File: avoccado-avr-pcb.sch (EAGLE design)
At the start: 32 parts, among them IC1 MCP1703CB, Q1 #MHz, Q2 MOSFET-NCHANNEL2N7002PW, U1 ATMEGA168#, U2 MCP73831, X1 Micro USB

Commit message: squeezed the headers together to make the PCB even thinner
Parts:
- removed C2: 0.1uF, SparkFun:CAP0402
- removed JP6, JP7: M12PTH, SparkFun:M12PTH
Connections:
- net A0: no longer JP6.8
- net A1: no longer JP6.7
- net A2: no longer JP6.6
- net A3: no longer JP6.5
- net D10: no longer JP6.12
- net D2: no longer JP7.8
- net D3: no longer JP7.7
- net D4: no longer JP7.6
- net D5-VIBR: no longer JP7.5
- net D6: no longer JP7.4
- net D7: no longer JP7.3
- net D8: no longer JP7.2
- net D9: no longer JP7.1
- net DTR: no longer C2.2
- net GND: no longer JP6.2, JP7.9
- net MISO: no longer JP6.10
- net MOSI: no longer JP6.11
- net RAW: no longer JP6.1
- net RESET: no longer C2.1, JP6.3, JP7.10
- net RXI: no longer JP7.11
- net SCK: no longer JP6.9
- net TXO: no longer JP7.12
- net VCC: no longer JP6.4
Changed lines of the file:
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@@
 <part name="U$2" library="SparkFun" deviceset="FIDUCIAL" device="1X2"/>
 <part name="U$4" library="SparkFun" deviceset="FIDUCIAL" device="1X2"/>
-<part name="JP6" library="SparkFun" deviceset="M12" device="PTH" value=""/>
-<part name="JP7" library="SparkFun" deviceset="M12" device="PTH" value=""/>
 <part name="Q1" library="SparkFun" deviceset="RESONATOR" device="SMD" value="#MHz"/>
 <part name="GND4" library="SparkFun" deviceset="GND" device=""/>
@@
 <part name="GND5" library="SparkFun" deviceset="GND" device=""/>
 <part name="JP1" library="SparkFun" deviceset="ARDUINO_SERIAL_PROGRAM" device="PTH" value="FTDI Basic"/>
-<part name="C2" library="SparkFun" deviceset="CAP" device="0402" value="0.1uF"/>
 <part name="Q2" library="SparkFun-DiscreteSemi" deviceset="MOSFET-NCHANNEL" device="2N7002PW"/>
 <part name="R1" library="SparkFun-Passives" deviceset="RESISTOR" device="0805-RES" value="1K"/>
@@
 <instance part="U$2" gate="G$1" x="236.22" y="25.4"/>
 <instance part="U$4" gate="G$1" x="241.3" y="25.4"/>
-<instance part="JP6" gate="G$1" x="134.62" y="58.42" rot="R180"/>
-<instance part="JP7" gate="G$1" x="48.26" y="60.96"/>
 <instance part="Q1" gate="G$1" x="165.1" y="127" smashed="yes" rot="MR90">
 <attribute name="NAME" x="162.306" y="123.444" size="1.778" layer="95" rot="MR180"/>
@@
 <instance part="GND5" gate="1" x="165.1" y="93.98"/>
 <instance part="JP1" gate="G$1" x="25.4" y="66.04"/>
-<instance part="C2" gate="G$1" x="132.08" y="154.94" smashed="yes" rot="R270">
-<attribute name="NAME" x="131.953" y="155.956" size="1.778" layer="95" rot="R90"/>
-<attribute name="VALUE" x="136.779" y="155.956" size="1.778" layer="96" rot="R90"/>
-</instance>
 <instance part="Q2" gate="G$1" x="48.26" y="104.14"/>
 <instance part="R1" gate="G$1" x="30.48" y="104.14"/>
@@
 <segment>
 <label x="78.74" y="66.04" size="1.778" layer="95"/>
-<pinref part="JP7" gate="G$1" pin="9"/>
 <wire x1="58.42" y1="66.04" x2="69.85" y2="66.04" width="0.1524" layer="91"/>
 <pinref part="JP11" gate="G$1" pin="1"/>
@@
 <segment>
 <label x="96.52" y="71.12" size="1.778" layer="95"/>
-<pinref part="JP6" gate="G$1" pin="2"/>
 <wire x1="124.46" y1="71.12" x2="110.49" y2="71.12" width="0.1524" layer="91"/>
 <pinref part="JP3" gate="G$1" pin="2"/>
@@
 <segment>
 <label x="78.74" y="68.58" size="1.778" layer="95"/>
-<pinref part="JP7" gate="G$1" pin="10"/>
 <wire x1="58.42" y1="68.58" x2="69.85" y2="68.58" width="0.1524" layer="91"/>
 <pinref part="JP11" gate="G$1" pin="2"/>
@@
 <segment>
 <label x="96.52" y="68.58" size="1.778" layer="95"/>
-<pinref part="JP6" gate="G$1" pin="3"/>
 <wire x1="124.46" y1="68.58" x2="110.49" y2="68.58" width="0.1524" layer="91"/>
 <pinref part="JP3" gate="G$1" pin="3"/>
@@
 <wire x1="167.64" y1="154.94" x2="142.24" y2="154.94" width="0.1524" layer="91"/>
 <wire x1="142.24" y1="157.48" x2="142.24" y2="154.94" width="0.1524" layer="91"/>
-<wire x1="142.24" y1="154.94" x2="137.16" y2="154.94" width="0.1524" layer="91"/>
-<junction x="142.24" y="154.94"/>
 <label x="152.4" y="154.94" size="1.778" layer="95"/>
 <pinref part="U1" gate="G$1" pin="PC6(/RESET)"/>
 <pinref part="R2" gate="G$1" pin="1"/>
-<pinref part="C2" gate="G$1" pin="1"/>
 </segment>
 </net>
@@
 <segment>
 <label x="96.52" y="53.34" size="1.778" layer="95"/>
-<pinref part="JP6" gate="G$1" pin="9"/>
 <wire x1="124.46" y1="53.34" x2="110.49" y2="53.34" width="0.1524" layer="91"/>
 <pinref part="JP8" gate="G$1" pin="1"/>
@@
 <segment>
 <label x="96.52" y="50.8" size="1.778" layer="95"/>
-<pinref part="JP6" gate="G$1" pin="10"/>
 <wire x1="124.46" y1="50.8" x2="110.49" y2="50.8" width="0.1524" layer="91"/>
 <pinref part="JP8" gate="G$1" pin="2"/>
@@
 <segment>
 <label x="96.52" y="48.26" size="1.778" layer="95"/>
-<pinref part="JP6" gate="G$1" pin="11"/>
 <wire x1="124.46" y1="48.26" x2="110.49" y2="48.26" width="0.1524" layer="91"/>
 <pinref part="JP8" gate="G$1" pin="3"/>
@@
 <segment>
 <label x="78.74" y="73.66" size="1.778" layer="95"/>
-<pinref part="JP7" gate="G$1" pin="12"/>
 <wire x1="58.42" y1="73.66" x2="69.85" y2="73.66" width="0.1524" layer="91"/>
 <pinref part="JP11" gate="G$1" pin="4"/>
@@
 <segment>
 <label x="96.52" y="66.04" size="1.778" layer="95"/>
-<pinref part="JP6" gate="G$1" pin="4"/>
 <wire x1="124.46" y1="66.04" x2="110.49" y2="66.04" width="0.1524" layer="91"/>
 <pinref part="JP3" gate="G$1" pin="4"/>
@@
 <segment>
 <label x="96.52" y="73.66" size="1.778" layer="95"/>
-<pinref part="JP6" gate="G$1" pin="1"/>
 <wire x1="124.46" y1="73.66" x2="110.49" y2="73.66" width="0.1524" layer="91"/>
 <pinref part="JP3" gate="G$1" pin="1"/>
@@
 <segment>
 <label x="78.74" y="45.72" size="1.778" layer="95"/>
-<pinref part="JP7" gate="G$1" pin="1"/>
 <wire x1="58.42" y1="45.72" x2="69.85" y2="45.72" width="0.1524" layer="91"/>
 <pinref part="JP9" gate="G$1" pin="1"/>
@@
 <segment>
 <label x="78.74" y="48.26" size="1.778" layer="95"/>
-<pinref part="JP7" gate="G$1" pin="2"/>
 <wire x1="83.82" y1="48.26" x2="69.85" y2="48.26" width="0.1524" layer="91"/>
 <pinref part="JP9" gate="G$1" pin="2"/>
@@
 <segment>
 <label x="96.52" y="63.5" size="1.778" layer="95"/>
-<pinref part="JP6" gate="G$1" pin="5"/>
 <wire x1="124.46" y1="63.5" x2="110.49" y2="63.5" width="0.1524" layer="91"/>
 <pinref part="JP5" gate="G$1" pin="1"/>
@@
 <segment>
 <label x="96.52" y="60.96" size="1.778" layer="95"/>
-<pinref part="JP6" gate="G$1" pin="6"/>
 <wire x1="124.46" y1="60.96" x2="110.49" y2="60.96" width="0.1524" layer="91"/>
 <pinref part="JP5" gate="G$1" pin="2"/>
@@
 <segment>
 <label x="96.52" y="58.42" size="1.778" layer="95"/>
-<pinref part="JP6" gate="G$1" pin="7"/>
 <wire x1="124.46" y1="58.42" x2="110.49" y2="58.42" width="0.1524" layer="91"/>
 <pinref part="JP5" gate="G$1" pin="3"/>
@@
 <segment>
 <label x="96.52" y="55.88" size="1.778" layer="95"/>
-<pinref part="JP6" gate="G$1" pin="8"/>
 <wire x1="124.46" y1="55.88" x2="110.49" y2="55.88" width="0.1524" layer="91"/>
 <pinref part="JP5" gate="G$1" pin="4"/>
@@
 <segment>
 <label x="78.74" y="63.5" size="1.778" layer="95"/>
-<pinref part="JP7" gate="G$1" pin="8"/>
 <wire x1="58.42" y1="63.5" x2="69.85" y2="63.5" width="0.1524" layer="91"/>
 <pinref part="JP10" gate="G$1" pin="4"/>
@@
 <segment>
 <label x="78.74" y="60.96" size="1.778" layer="95"/>
-<pinref part="JP7" gate="G$1" pin="7"/>
 <wire x1="83.82" y1="60.96" x2="69.85" y2="60.96" width="0.1524" layer="91"/>
 <pinref part="JP10" gate="G$1" pin="3"/>
@@
 <segment>
 <label x="78.74" y="58.42" size="1.778" layer="95"/>
-<pinref part="JP7" gate="G$1" pin="6"/>
 <wire x1="83.82" y1="58.42" x2="69.85" y2="58.42" width="0.1524" layer="91"/>
 <pinref part="JP10" gate="G$1" pin="2"/>
@@
 <segment>
 <label x="78.74" y="55.88" size="1.778" layer="95"/>
-<pinref part="JP7" gate="G$1" pin="5"/>
 <wire x1="58.42" y1="55.88" x2="69.85" y2="55.88" width="0.1524" layer="91"/>
 <pinref part="JP10" gate="G$1" pin="1"/>
@@
 <segment>
 <label x="78.74" y="53.34" size="1.778" layer="95"/>
-<pinref part="JP7" gate="G$1" pin="4"/>
 <wire x1="58.42" y1="53.34" x2="69.85" y2="53.34" width="0.1524" layer="91"/>
 <pinref part="JP9" gate="G$1" pin="4"/>
@@
 <segment>
 <label x="78.74" y="50.8" size="1.778" layer="95"/>
-<pinref part="JP7" gate="G$1" pin="3"/>
 <wire x1="58.42" y1="50.8" x2="69.85" y2="50.8" width="0.1524" layer="91"/>
 <pinref part="JP9" gate="G$1" pin="3"/>
@@
 <segment>
 <label x="96.52" y="45.72" size="1.778" layer="95"/>
-<pinref part="JP6" gate="G$1" pin="12"/>
 <wire x1="124.46" y1="45.72" x2="110.49" y2="45.72" width="0.1524" layer="91"/>
 <pinref part="JP8" gate="G$1" pin="4"/>
@@
 <pinref part="JP1" gate="G$1" pin="DTR"/>
 </segment>
-<segment>
-<wire x1="129.54" y1="154.94" x2="121.92" y2="154.94" width="0.1524" layer="91"/>
-<label x="121.92" y="154.94" size="1.778" layer="95"/>
-<pinref part="C2" gate="G$1" pin="2"/>
-</segment>
 </net>
 <net name="RXI" class="0">
@@
 <segment>
 <label x="78.74" y="71.12" size="1.778" layer="95"/>
-<pinref part="JP7" gate="G$1" pin="11"/>
 <wire x1="58.42" y1="71.12" x2="69.85" y2="71.12" width="0.1524" layer="91"/>
 <pinref part="JP11" gate="G$1" pin="3"/>

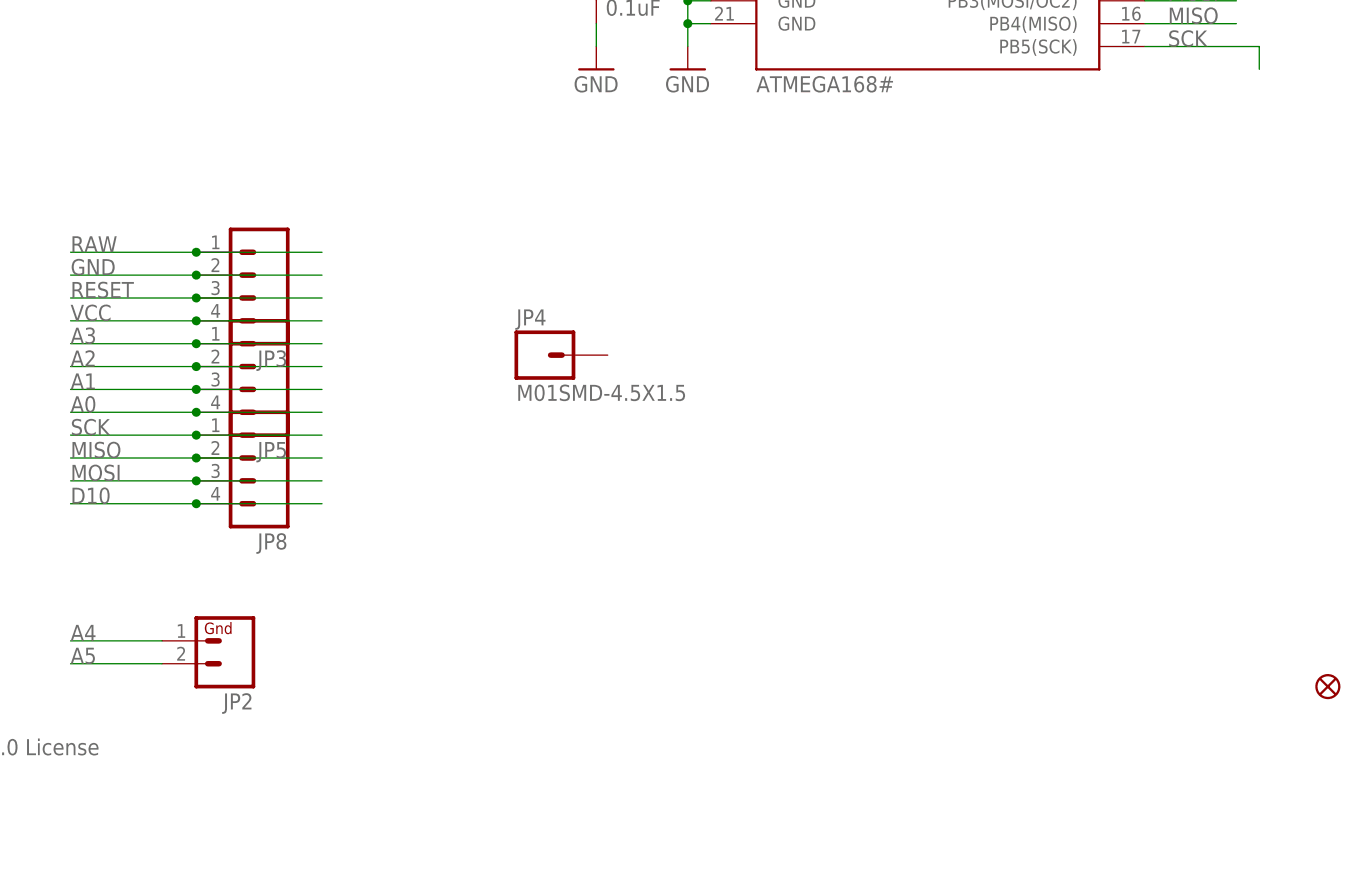
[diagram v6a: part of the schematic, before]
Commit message: add NRF24 header wip
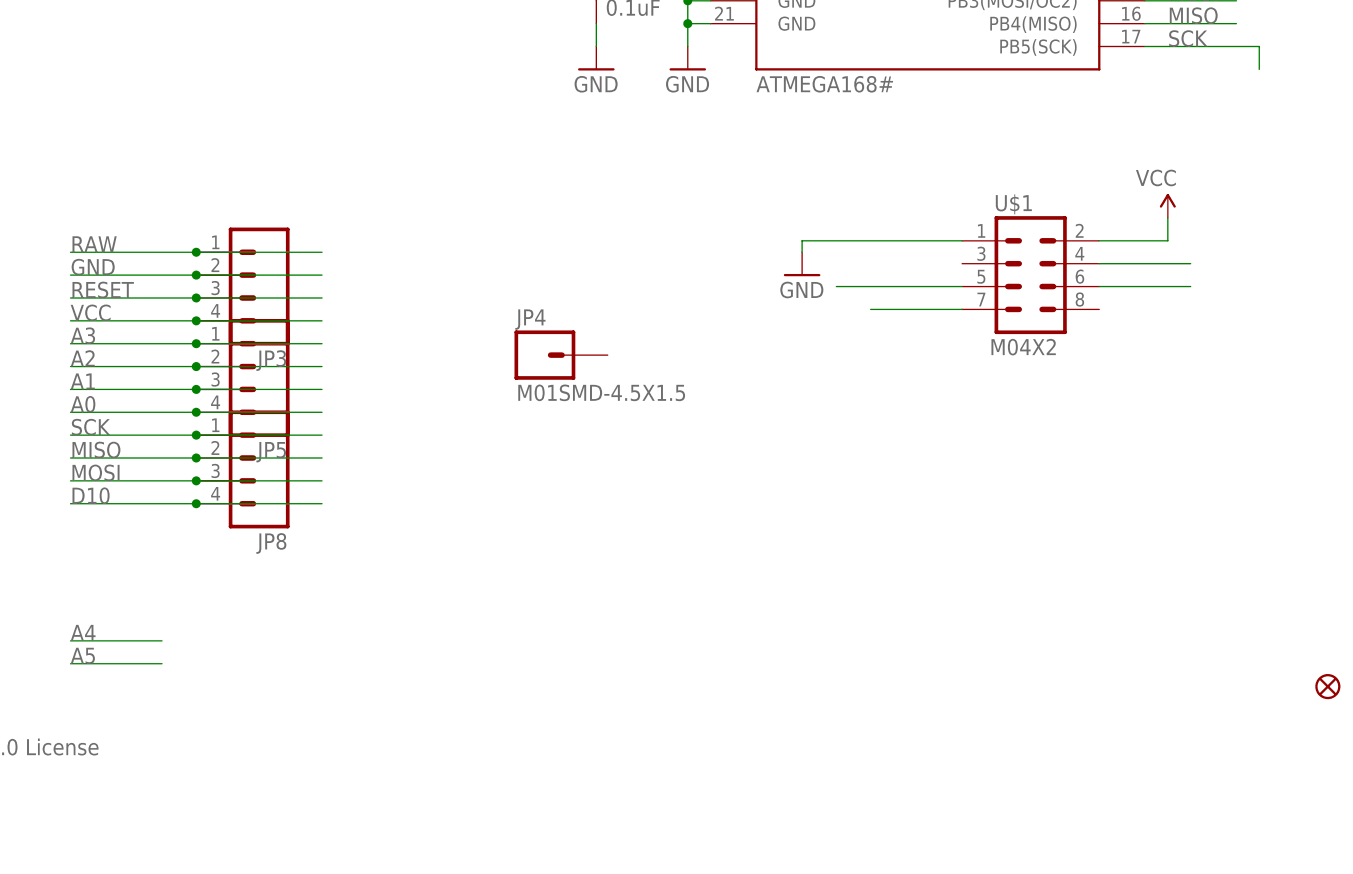
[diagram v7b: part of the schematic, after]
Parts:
- removed JP2: (no value), SparkFun:M02PTH
- added U$1: M04X2, SparkFun-Connectors:M04X2
- R1, R5: device SparkFun-Passives:RESISTOR0805-RES -> SparkFun-Resistors:RESISTOR0603
- R2: device SparkFun:RESISTOR0402 -> SparkFun-Resistors:RESISTOR0603
- R3, R4: device SparkFun-Resistors:RESISTOR0805-RES -> SparkFun-Resistors:RESISTOR0603
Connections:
- new net 3.3V: U$1.2
- net A4: no longer JP2.1
- net A5: no longer JP2.2
- net D10: now also U$1.4
- net GND: now also U$1.1
- net MISO: now also U$1.7
- net MOSI: now also U$1.6
- net SCK: now also U$1.5
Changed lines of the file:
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@@
 <part name="GND25" library="SparkFun" deviceset="GND" device=""/>
 <part name="GND26" library="SparkFun" deviceset="GND" device=""/>
-<part name="R2" library="SparkFun" deviceset="RESISTOR" device="0402" value="10K"/>
+<part name="R2" library="SparkFun-Resistors" deviceset="RESISTOR" device="0603" value="10K"/>
 <part name="C3" library="SparkFun" deviceset="CAP" device="0402" value="0.1uF"/>
 <part name="GND1" library="SparkFun" deviceset="GND" device=""/>
@@
 <part name="Q1" library="SparkFun" deviceset="RESONATOR" device="SMD" value="#MHz"/>
 <part name="GND4" library="SparkFun" deviceset="GND" device=""/>
-<part name="JP2" library="SparkFun" deviceset="M02" device="PTH"/>
 <part name="U1" library="SparkFun" deviceset="ATMEGA168" device="" value="ATMEGA168#"/>
 <part name="P+1" library="SparkFun" deviceset="3.3V" device="" value="VCC"/>
@@
 <part name="JP1" library="SparkFun" deviceset="ARDUINO_SERIAL_PROGRAM" device="PTH" value="FTDI Basic"/>
 <part name="Q2" library="SparkFun-DiscreteSemi" deviceset="MOSFET-NCHANNEL" device="2N7002PW"/>
-<part name="R1" library="SparkFun-Passives" deviceset="RESISTOR" device="0805-RES" value="1K"/>
+<part name="R1" library="SparkFun-Resistors" deviceset="RESISTOR" device="0603" value="1K"/>
 <part name="IC1" library="linear" deviceset="MCP1703" device="CB"/>
 <part name="U2" library="SparkFun" deviceset="MCP73831" device=""/>
 <part name="GND2" library="SparkFun" deviceset="GND" device=""/>
-<part name="R3" library="SparkFun-Resistors" deviceset="RESISTOR" device="0805-RES" value="2K"/>
+<part name="R3" library="SparkFun-Resistors" deviceset="RESISTOR" device="0603" value="2K"/>
 <part name="GND3" library="SparkFun" deviceset="GND" device=""/>
 <part name="D1" library="SparkFun" deviceset="LED" device="0603" value="CHARGE LED"/>
@@
 <part name="X1" library="SparkFun" deviceset="USB" device="-MICROB" value="Micro USB"/>
 <part name="C4" library="SparkFun-Capacitors" deviceset="4.7UF-6.3V-10%(0603)" device="0603" value="4.7uF"/>
-<part name="R4" library="SparkFun-Resistors" deviceset="RESISTOR" device="0805-RES" value="2K"/>
+<part name="R4" library="SparkFun-Resistors" deviceset="RESISTOR" device="0603" value="2K"/>
 <part name="GND6" library="SparkFun" deviceset="GND" device=""/>
 <part name="GND8" library="SparkFun" deviceset="GND" device=""/>
 <part name="GND9" library="SparkFun" deviceset="GND" device=""/>
-<part name="R5" library="SparkFun-Passives" deviceset="RESISTOR" device="0805-RES" value="1M"/>
+<part name="R5" library="SparkFun-Resistors" deviceset="RESISTOR" device="0603" value="1M"/>
 <part name="JP4" library="SparkFun-Connectors" deviceset="M01" device="SMD-4.5X1.5"/>
 <part name="JP3" library="smd-pads" deviceset="M04" device="SMD1X4"/>
@@
 <part name="JP10" library="smd-pads" deviceset="M04" device="SMD1X4"/>
 <part name="JP11" library="smd-pads" deviceset="M04" device="SMD1X4"/>
+<part name="U$1" library="SparkFun-Connectors" deviceset="M04X2" device=""/>
+<part name="GND10" library="SparkFun" deviceset="GND" device=""/>
+<part name="P+2" library="SparkFun" deviceset="3.3V" device="" value="VCC"/>
 </parts>
 <sheets>
@@
 </instance>
 <instance part="GND4" gate="1" x="154.94" y="121.92"/>
-<instance part="JP2" gate="G$1" x="114.3" y="30.48" rot="R180"/>
 <instance part="U1" gate="G$1" x="190.5" y="129.54" smashed="yes">
 <attribute name="NAME" x="172.974" y="158.242" size="1.778" layer="95"/>
@@
 <instance part="JP10" gate="G$1" x="64.77" y="58.42"/>
 <instance part="JP11" gate="G$1" x="64.77" y="68.58"/>
+<instance part="U$1" gate="G$1" x="203.2" y="69.85"/>
+<instance part="GND10" gate="1" x="177.8" y="71.12"/>
+<instance part="P+2" gate="G$1" x="218.44" y="77.47" smashed="yes">
+<attribute name="VALUE" x="214.884" y="81.026" size="1.778" layer="96"/>
+</instance>
 </instances>
 <busses>
@@
 <wire x1="38.1" y1="90.17" x2="38.1" y2="91.44" width="0.1524" layer="91"/>
 </segment>
+<segment>
+<pinref part="U$1" gate="G$1" pin="1"/>
+<wire x1="195.58" y1="74.93" x2="177.8" y2="74.93" width="0.2032" layer="91"/>
+<pinref part="GND10" gate="1" pin="GND"/>
+<wire x1="177.8" y1="74.93" x2="177.8" y2="73.66" width="0.2032" layer="91"/>
+</segment>
 </net>
 <net name="AREF" class="0">
@@
 <pinref part="U1" gate="G$1" pin="PB5(SCK)"/>
 </segment>
+<segment>
+<wire x1="181.61" y1="69.85" x2="195.58" y2="69.85" width="0.1524" layer="91"/>
+<pinref part="U$1" gate="G$1" pin="5"/>
+</segment>
 </net>
 <net name="MISO" class="0">
@@
 <pinref part="U1" gate="G$1" pin="PB4(MISO)"/>
 </segment>
+<segment>
+<wire x1="185.42" y1="67.31" x2="195.58" y2="67.31" width="0.1524" layer="91"/>
+<pinref part="U$1" gate="G$1" pin="7"/>
+</segment>
 </net>
 <net name="MOSI" class="0">
@@
 <label x="218.44" y="101.6" size="1.778" layer="95"/>
 <pinref part="U1" gate="G$1" pin="PB3(MOSI/OC2)"/>
+</segment>
+<segment>
+<wire x1="210.82" y1="69.85" x2="220.98" y2="69.85" width="0.1524" layer="91"/>
+<pinref part="U$1" gate="G$1" pin="6"/>
 </segment>
 </net>
@@
 <wire x1="106.68" y1="27.94" x2="96.52" y2="27.94" width="0.1524" layer="91"/>
 <label x="96.52" y="27.94" size="1.778" layer="95"/>
-<pinref part="JP2" gate="G$1" pin="2"/>
 </segment>
 <segment>
@@
 <wire x1="106.68" y1="30.48" x2="96.52" y2="30.48" width="0.1524" layer="91"/>
 <label x="96.52" y="30.48" size="1.778" layer="95"/>
-<pinref part="JP2" gate="G$1" pin="1"/>
 </segment>
 <segment>
@@
 <label x="218.44" y="104.14" size="1.778" layer="95"/>
 <pinref part="U1" gate="G$1" pin="PB2(SS/OC1B)"/>
+</segment>
+<segment>
+<wire x1="210.82" y1="72.39" x2="220.98" y2="72.39" width="0.1524" layer="91"/>
+<pinref part="U$1" gate="G$1" pin="4"/>
 </segment>
 </net>
@@
 </segment>
 </net>
+<net name="3.3V" class="0">
+<segment>
+<pinref part="P+2" gate="G$1" pin="3.3V"/>
+<wire x1="218.44" y1="77.47" x2="218.44" y2="74.93" width="0.2032" layer="91"/>
+<pinref part="U$1" gate="G$1" pin="2"/>
+<wire x1="218.44" y1="74.93" x2="210.82" y2="74.93" width="0.2032" layer="91"/>
+</segment>
+</net>
